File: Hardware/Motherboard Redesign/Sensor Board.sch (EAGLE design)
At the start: 28 parts, among them J1 U.FL, Q1 Q_LM35TO-92

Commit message: Responding with a finished sensor board.
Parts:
- removed Q1: Q_LM35TO-92, MRDT-2014-All:Q_LM35TO-92
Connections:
- removed net A8: Q1.OUT, U$1.D8/A8
- net +3V3: no longer Q1.VIN
- net GND: no longer Q1.GND
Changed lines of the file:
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@@
 <part name="GND13" library="supply1" deviceset="GND" device=""/>
 <part name="+3V16" library="supply1" deviceset="+3V3" device=""/>
-<part name="Q1" library="MRDT-2014-All" deviceset="Q_LM35" device="TO-92"/>
 <part name="IC1" library="Spark" deviceset="MCP1825S" device="-SOT223"/>
 <part name="SUPPLY1" library="SparkFun-Aesthetics" deviceset="5V" device=""/>
@@
 <part name="GND10" library="supply1" deviceset="GND" device=""/>
 <part name="+3V6" library="supply1" deviceset="+3V3" device=""/>
-<part name="+3V7" library="supply1" deviceset="+3V3" device=""/>
-<part name="GND11" library="supply1" deviceset="GND" device=""/>
 <part name="S1" library="SparkFun-Electromechanical" deviceset="STANDOFF_ELECTRICAL" device=""/>
 <part name="S2" library="SparkFun-Electromechanical" deviceset="STANDOFF_ELECTRICAL" device=""/>
@@
 <instance part="GND13" gate="1" x="149.86" y="101.6"/>
 <instance part="+3V16" gate="G$1" x="149.86" y="127"/>
-<instance part="Q1" gate="G$1" x="198.12" y="66.04"/>
 <instance part="IC1" gate="G$1" x="259.08" y="88.9"/>
 <instance part="SUPPLY1" gate="G$1" x="246.38" y="88.9" rot="R90"/>
@@
 <instance part="GND10" gate="1" x="261.62" y="76.2"/>
 <instance part="+3V6" gate="G$1" x="274.32" y="88.9" rot="R270"/>
-<instance part="+3V7" gate="G$1" x="190.5" y="71.12" rot="R90"/>
-<instance part="GND11" gate="1" x="190.5" y="66.04" rot="R270"/>
 <instance part="S1" gate="G$1" x="35.56" y="172.72" rot="R270"/>
 <instance part="S2" gate="G$1" x="48.26" y="172.72" rot="R270"/>
@@
 </segment>
 <segment>
-<pinref part="Q1" gate="G$1" pin="GND"/>
-<pinref part="GND11" gate="1" pin="GND"/>
-</segment>
-<segment>
 <pinref part="S2" gate="G$1" pin="P$1"/>
 <pinref part="GND14" gate="1" pin="GND"/>
@@
 </segment>
 <segment>
-<pinref part="Q1" gate="G$1" pin="VIN"/>
-<pinref part="+3V7" gate="G$1" pin="+3V3"/>
-</segment>
-<segment>
 <pinref part="JP1" gate="G$1" pin="2"/>
 <pinref part="+3V8" gate="G$1" pin="+3V3"/>
@@
 </segment>
 </net>
-<net name="A8" class="0">
-<segment>
-<pinref part="U$1" gate="G$1" pin="D8/A8"/>
-<wire x1="60.96" y1="76.2" x2="66.04" y2="76.2" width="0.1524" layer="91"/>
-<label x="66.04" y="76.2" size="1.778" layer="95"/>
-</segment>
-<segment>
-<pinref part="Q1" gate="G$1" pin="OUT"/>
-<wire x1="210.82" y1="68.58" x2="215.9" y2="68.58" width="0.1524" layer="91"/>
-<label x="215.9" y="68.58" size="1.778" layer="95"/>
-</segment>
-</net>

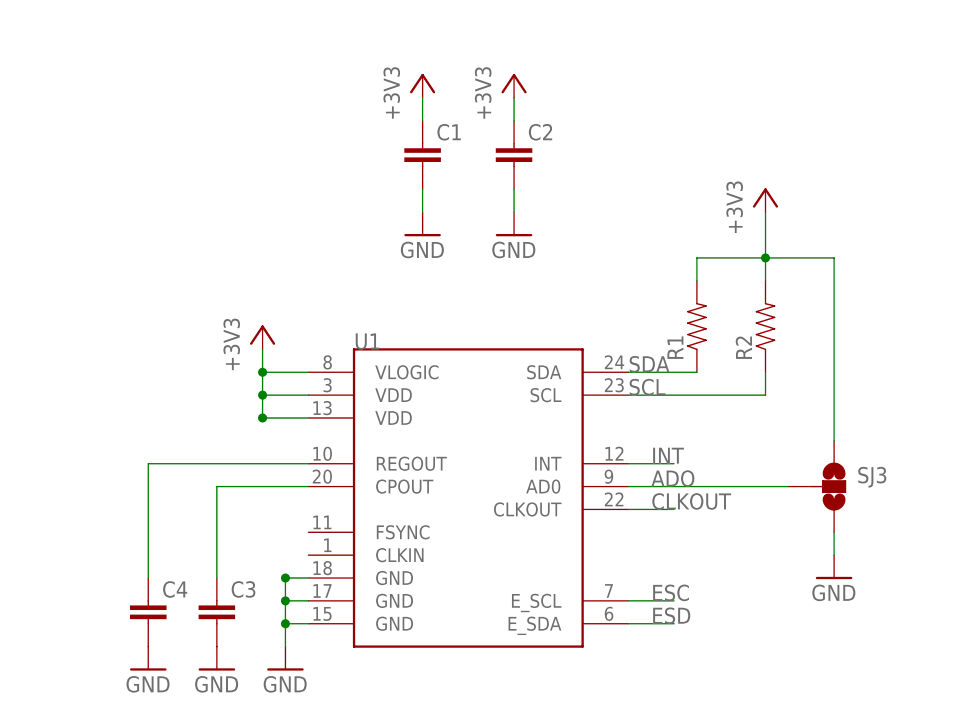
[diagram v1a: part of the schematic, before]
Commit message: added magnetometer passive component values
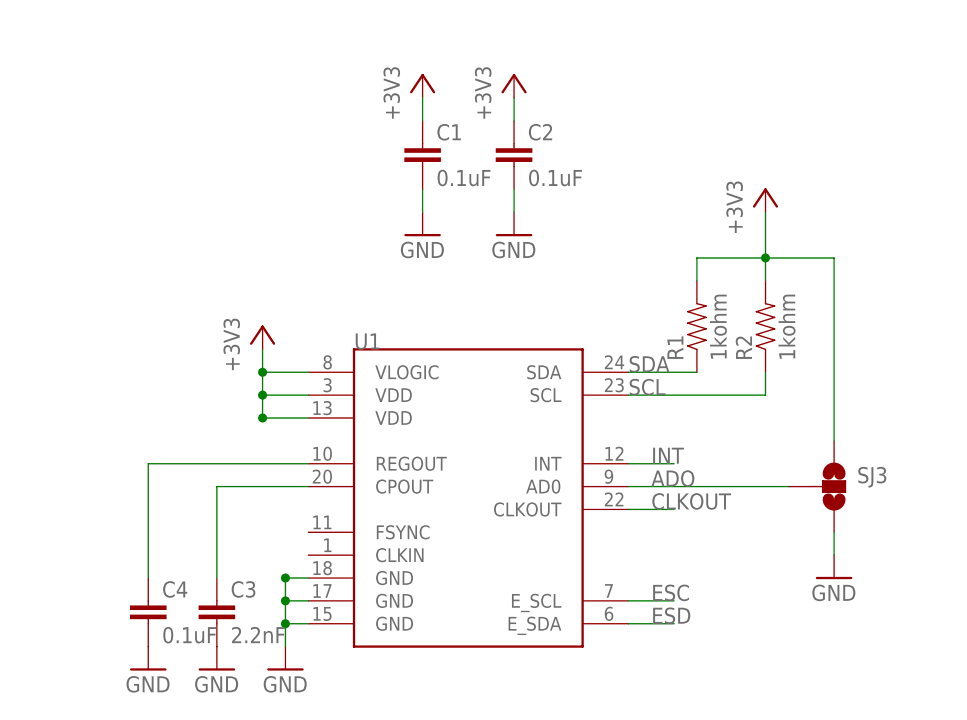
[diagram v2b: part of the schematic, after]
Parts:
- C1, C2, C4: value (none) -> 0.1uF
- C3: value (none) -> 2.2nF
- R1, R2: value (none) -> 1kohm
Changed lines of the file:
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@@
 <?xml version="1.0" encoding="utf-8"?>
 <!DOCTYPE eagle SYSTEM "eagle.dtd">
-<eagle version="7.2.0">
+<eagle version="6.5.0">
 <drawing>
 <settings>
@@
 <part name="+3V1" library="supply1" deviceset="+3V3" device=""/>
 <part name="+3V2" library="supply1" deviceset="+3V3" device=""/>
-<part name="C1" library="SparkFun-Capacitors" deviceset="CAP" device="1206"/>
-<part name="C2" library="SparkFun-Capacitors" deviceset="CAP" device="1206"/>
-<part name="C3" library="SparkFun-Capacitors" deviceset="CAP" device="1206"/>
-<part name="C4" library="SparkFun-Capacitors" deviceset="CAP" device="1206"/>
-<part name="R1" library="SparkFun-Resistors" deviceset="RESISTOR" device="1206"/>
-<part name="R2" library="SparkFun-Resistors" deviceset="RESISTOR" device="1206"/>
+<part name="C1" library="SparkFun-Capacitors" deviceset="CAP" device="1206" value="0.1uF"/>
+<part name="C2" library="SparkFun-Capacitors" deviceset="CAP" device="1206" value="0.1uF"/>
+<part name="C3" library="SparkFun-Capacitors" deviceset="CAP" device="1206" value="2.2nF"/>
+<part name="C4" library="SparkFun-Capacitors" deviceset="CAP" device="1206" value="0.1uF"/>
+<part name="R1" library="SparkFun-Resistors" deviceset="RESISTOR" device="1206" value="1kohm"/>
+<part name="R2" library="SparkFun-Resistors" deviceset="RESISTOR" device="1206" value="1kohm"/>
 <part name="+3V3" library="supply1" deviceset="+3V3" device=""/>
 <part name="+3V4" library="supply1" deviceset="+3V3" device=""/>

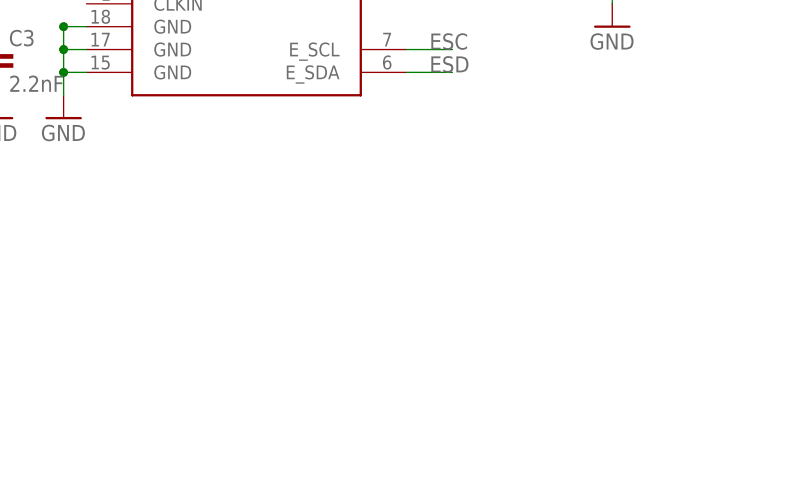
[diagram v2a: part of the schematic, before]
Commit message: edited sensor board eagle file and code to URC 2015 ready
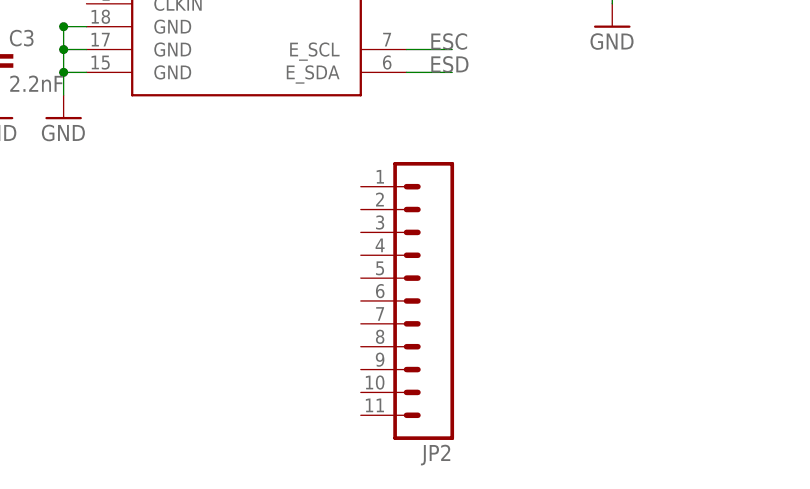
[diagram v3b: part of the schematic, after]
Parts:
- added JP2: (no value), SparkFun-Connectors:M11PTH
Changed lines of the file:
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@@
 <layers>
 <layer number="1" name="Top" color="4" fill="1" visible="no" active="no"/>
+<layer number="2" name="Route2" color="1" fill="3" visible="no" active="no"/>
+<layer number="3" name="Route3" color="4" fill="3" visible="no" active="no"/>
+<layer number="4" name="Route4" color="1" fill="4" visible="no" active="no"/>
+<layer number="5" name="Route5" color="4" fill="4" visible="no" active="no"/>
+<layer number="6" name="Route6" color="1" fill="8" visible="no" active="no"/>
+<layer number="7" name="Route7" color="4" fill="8" visible="no" active="no"/>
+<layer number="8" name="Route8" color="1" fill="2" visible="no" active="no"/>
+<layer number="9" name="Route9" color="4" fill="2" visible="no" active="no"/>
+<layer number="10" name="Route10" color="1" fill="7" visible="no" active="no"/>
+<layer number="11" name="Route11" color="4" fill="7" visible="no" active="no"/>
+<layer number="12" name="Route12" color="1" fill="5" visible="no" active="no"/>
+<layer number="13" name="Route13" color="4" fill="5" visible="no" active="no"/>
+<layer number="14" name="Route14" color="1" fill="6" visible="no" active="no"/>
+<layer number="15" name="Route15" color="4" fill="6" visible="no" active="no"/>
 <layer number="16" name="Bottom" color="1" fill="1" visible="no" active="no"/>
 <layer number="17" name="Pads" color="2" fill="1" visible="no" active="no"/>
@@
 <part name="GND18" library="supply1" deviceset="GND" device=""/>
 <part name="+3V8" library="supply1" deviceset="+3V3" device=""/>
+<part name="JP2" library="SparkFun-Connectors" deviceset="M11" device="PTH"/>
 </parts>
 <sheets>
@@
 <instance part="GND18" gate="1" x="231.14" y="30.48"/>
 <instance part="+3V8" gate="G$1" x="228.6" y="30.48" rot="R180"/>
+<instance part="JP2" gate="G$1" x="157.48" y="-12.7" rot="R180"/>
 </instances>
 <busses>
